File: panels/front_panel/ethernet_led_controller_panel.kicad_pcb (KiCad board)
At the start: 2 copper layers, 100 x 60 mm, 0 parts

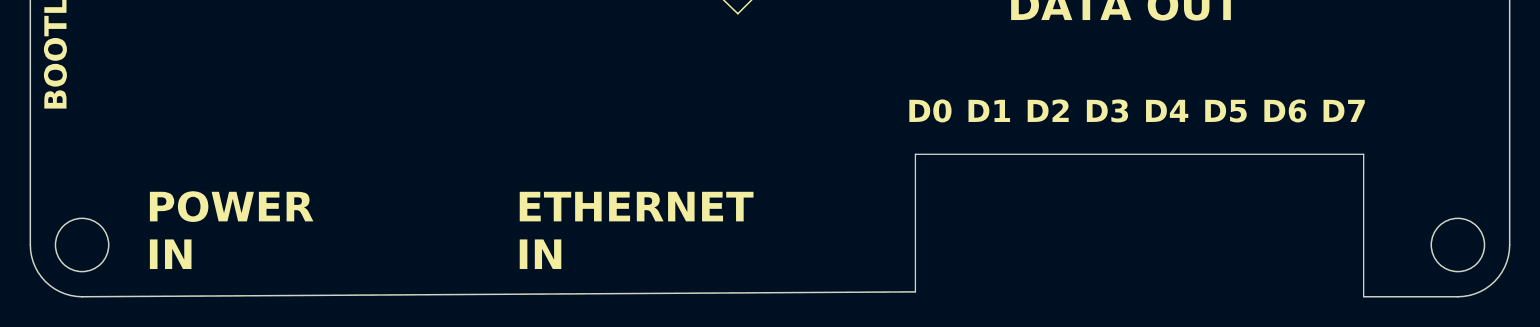
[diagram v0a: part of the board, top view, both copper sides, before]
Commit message: updated board to use 4x terminal blocks
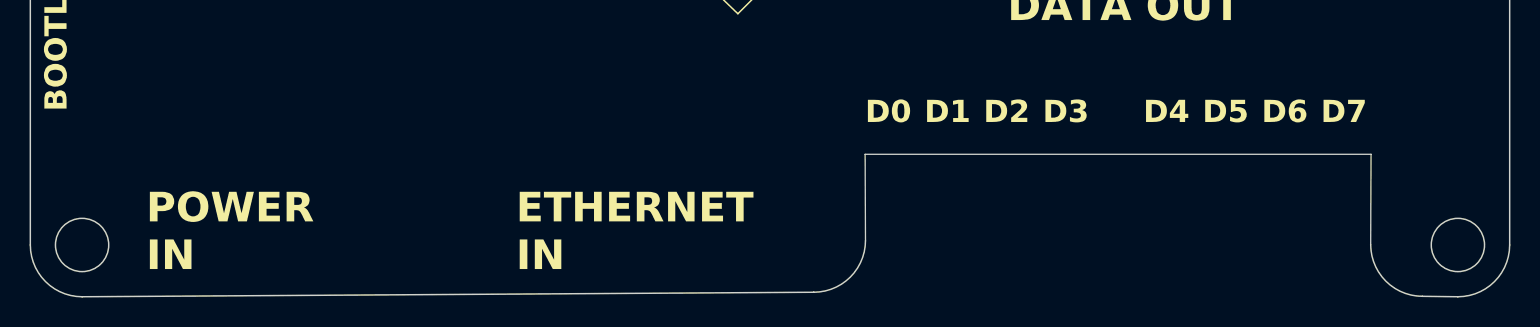
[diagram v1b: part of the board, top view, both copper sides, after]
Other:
- outline, holes or cut-outs redrawn
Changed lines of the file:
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@@
   (gr_line (start 189.17 62.63) (end 189.17 115.63)
     (stroke (width 0.1) (type default)) (layer "Edge.Cuts"))
-  (gr_line (start 149 118.8) (end 92.67 119.13)
+  (gr_line (start 142.125126 118.825126) (end 92.67 119.13)
     (stroke (width 0.1) (type default)) (layer "Edge.Cuts"))
-  (gr_line (start 185.67 119.13) (end 179.3 119.13)
+  (gr_line (start 185.67 119.13) (end 183.274874 119.1)
     (stroke (width 0.1) (type default)) (layer "Edge.Cuts"))
   (gr_circle (center 185.67 115.63) (end 183.87 115.63)
@@
   (gr_arc (start 89.17 62.63) (mid 90.195126 60.155126) (end 92.67 59.13)
     (stroke (width 0.1) (type default)) (layer "Edge.Cuts"))
+  (gr_arc (start 145.625126 115.325126) (mid 144.6 117.8) (end 142.125126 118.825126)
+    (stroke (width 0.1) (type default)) (layer "Edge.Cuts"))
+  (gr_arc (start 183.274874 119.1) (mid 180.8 118.074874) (end 179.774874 115.6)
+    (stroke (width 0.1) (type default)) (layer "Edge.Cuts"))
   (gr_arc (start 189.17 115.63) (mid 188.144874 118.104874) (end 185.67 119.13)
     (stroke (width 0.1) (type default)) (layer "Edge.Cuts"))
@@
   (gr_arc (start 185.67 59.13) (mid 188.144874 60.155126) (end 189.17 62.63)
     (stroke (width 0.1) (type default)) (layer "Edge.Cuts"))
-  (gr_line (start 149 109.5) (end 149 118.8)
+  (gr_line (start 145.6 109.5) (end 145.625126 115.325126)
     (stroke (width 0.05) (type default)) (layer "Edge.Cuts"))
   (gr_arc (start 92.67 119.13) (mid 90.195126 118.104874) (end 89.17 115.63)
     (stroke (width 0.1) (type default)) (layer "Edge.Cuts"))
-  (gr_line (start 179.3 119.13) (end 179.3 109.5)
+  (gr_line (start 179.774874 115.6) (end 179.8 109.5)
     (stroke (width 0.05) (type default)) (layer "Edge.Cuts"))
-  (gr_line (start 179.3 109.5) (end 149 109.5)
+  (gr_line (start 179.8 109.5) (end 145.6 109.5)
     (stroke (width 0.05) (type default)) (layer "Edge.Cuts"))
   (gr_line (start 92.67 59.13) (end 185.67 59.13)
@@
     (effects (font (size 1.5 1.5) (thickness 0.3) bold) (justify left bottom))
   )
-  (gr_text "D1" (at 152.4 107.5) (layer "F.SilkS")
+  (gr_text "D1" (at 149.6 107.5) (layer "F.SilkS")
     (effects (font (size 1.5 1.5) (thickness 0.3) bold) (justify left bottom))
   )
@@
     (effects (font (size 1.5 1.5) (thickness 0.3) bold) (justify left bottom))
   )
-  (gr_text "D3" (at 160.4 107.5) (layer "F.SilkS")
+  (gr_text "D3" (at 157.6 107.5) (layer "F.SilkS")
     (effects (font (size 1.5 1.5) (thickness 0.3) bold) (justify left bottom))
   )
@@
     (effects (font (size 1.3 1.3) (thickness 0.18)) (justify left bottom))
   )
-  (gr_text "D0" (at 148.4 107.5) (layer "F.SilkS")
+  (gr_text "D0" (at 145.6 107.5) (layer "F.SilkS")
     (effects (font (size 1.5 1.5) (thickness 0.3) bold) (justify left bottom))
   )
@@
     (effects (font (size 1.5 1.5) (thickness 0.3) bold) (justify left bottom))
   )
-  (gr_text "D2" (at 156.4 107.5) (layer "F.SilkS")
+  (gr_text "D2" (at 153.6 107.5) (layer "F.SilkS")
     (effects (font (size 1.5 1.5) (thickness 0.3) bold) (justify left bottom))
   )

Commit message: update hardware to v1_2_0
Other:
- outline, holes or cut-outs redrawn
- board text added: "LATERAL LED_CONTROLLER"
- board text added: "LATERAL_LED FRONT PANEL v1_2_0 cyberboy666 & tor"
- board text added: "RJ45 DATA OUT"
- board text removed: "LATERAL_LEDS FRONT PANEL v1_1_0 cyberboy666 & __"
- board text removed: "lateral leds controller"
